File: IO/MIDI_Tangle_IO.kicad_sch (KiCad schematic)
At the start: 14 parts, among them J1 Conn_01x08_Male, J2 Conn_01x08_Male, J3 Conn_01x08_Male, J4 Conn_01x08_Male, SW1 SW_SPST, SW2 SW_SPST, SW3 SW_SPST, SW4 SW_SPST, SW5 SW_SPST, SW6 SW_SPST, SW7 SW_SPST, SW8 SW_SPST

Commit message: Update PCB layout
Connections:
- net Butt1: now also J1.5 (Pin_5); no longer J1.3 (Pin_3)
- net Butt2: now also J1.6 (Pin_6); no longer J1.4 (Pin_4)
- net ButtSelX: now also J2.6 (Pin_6); no longer J1.5 (Pin_5)
- net GND: now also J1.7 (Pin_7), J3.8 (Pin_8); no longer J2.5 (Pin_5), J2.8 (Pin_8)
- net JackO1: now also J1.3 (Pin_3); no longer J1.7 (Pin_7)
- net JackO2: now also J1.4 (Pin_4); no longer J1.6 (Pin_6)
- net JackO4: now also J2.5 (Pin_5); no longer J2.6 (Pin_6)
- net at R1.1: now also J2.8 (Pin_8); no longer J3.8 (Pin_8)
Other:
- moved on the sheet: D1, R1

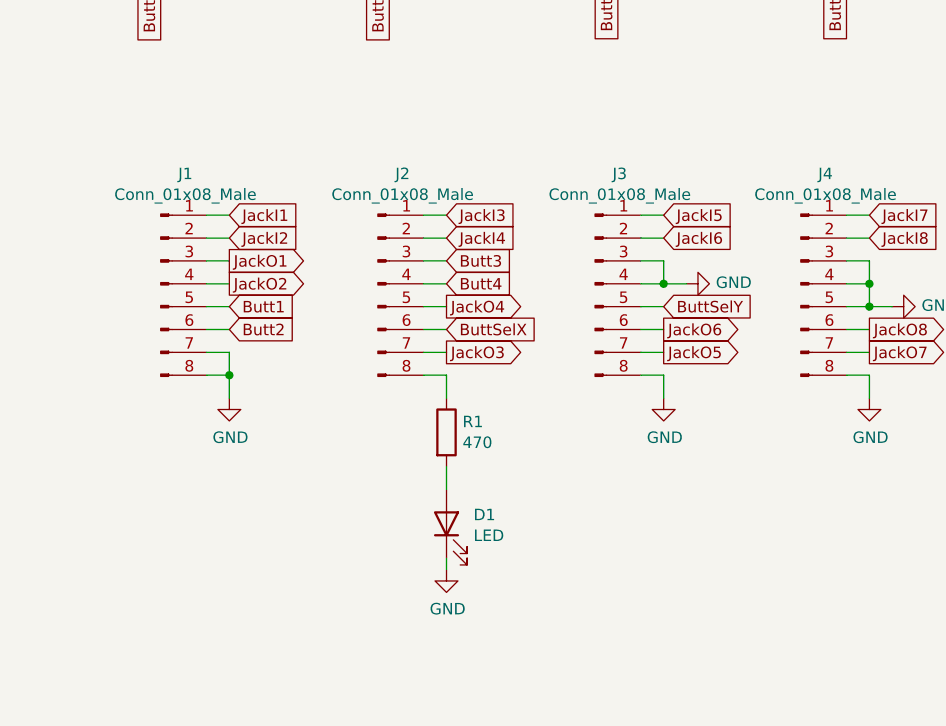
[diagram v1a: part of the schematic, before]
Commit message: Reduce output capacitive load
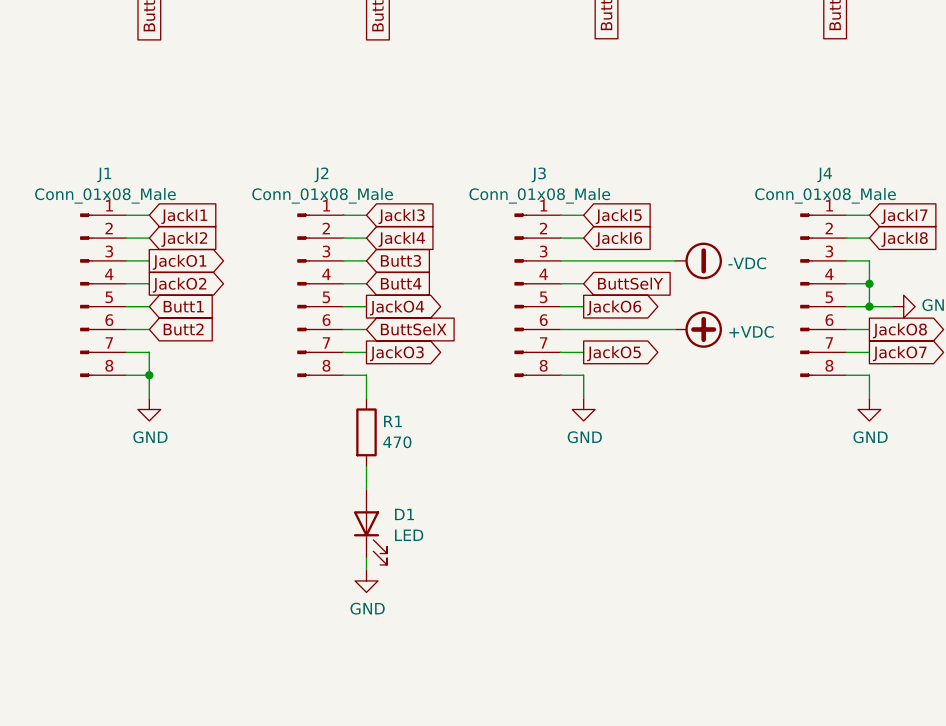
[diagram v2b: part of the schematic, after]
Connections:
- net ButtSelY: now also J3.4 (Pin_4); no longer J3.5 (Pin_5)
- net GND: no longer J3.3 (Pin_3), J3.4 (Pin_4)
- net JackO6: now also J3.5 (Pin_5); no longer J3.6 (Pin_6)
- new net +VDC: J3.6 (Pin_6)
- new net -VDC: J3.3 (Pin_3)
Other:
- moved on the sheet: D1, J1, J2, J3, R1

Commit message: Update sheet metadata
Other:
- company: (none) -> GuavTek
- title: (none) -> M2IDI_IO
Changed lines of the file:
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@@
 (kicad_sch (version 20230121) (generator eeschema)
   (paper "A4")
+  (title_block
+    (title "M2IDI_IO")
+    (date "2023-04-19")
+    (rev "1.1")
+    (company "GuavTek")
+  )
   (junction (at 59.69 57.15) (diameter 0) (color 0 0 0 0)
   )

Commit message: Fix metadata
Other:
- title: M2IDI_IO -> M2IDI - TANGLE IO
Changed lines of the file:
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@@
   (paper "A4")
   (title_block
-    (title "M2IDI_IO")
+    (title "M2IDI - TANGLE IO")
     (date "2023-04-19")
     (rev "1.1")
